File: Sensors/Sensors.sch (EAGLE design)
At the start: 32 parts, among them J2 JST_CONNECTOR, J6 JST_CONNECTOR, J7 JST_CONNECTOR, J8 JST_CONNECTOR, J9 JST_CONNECTOR

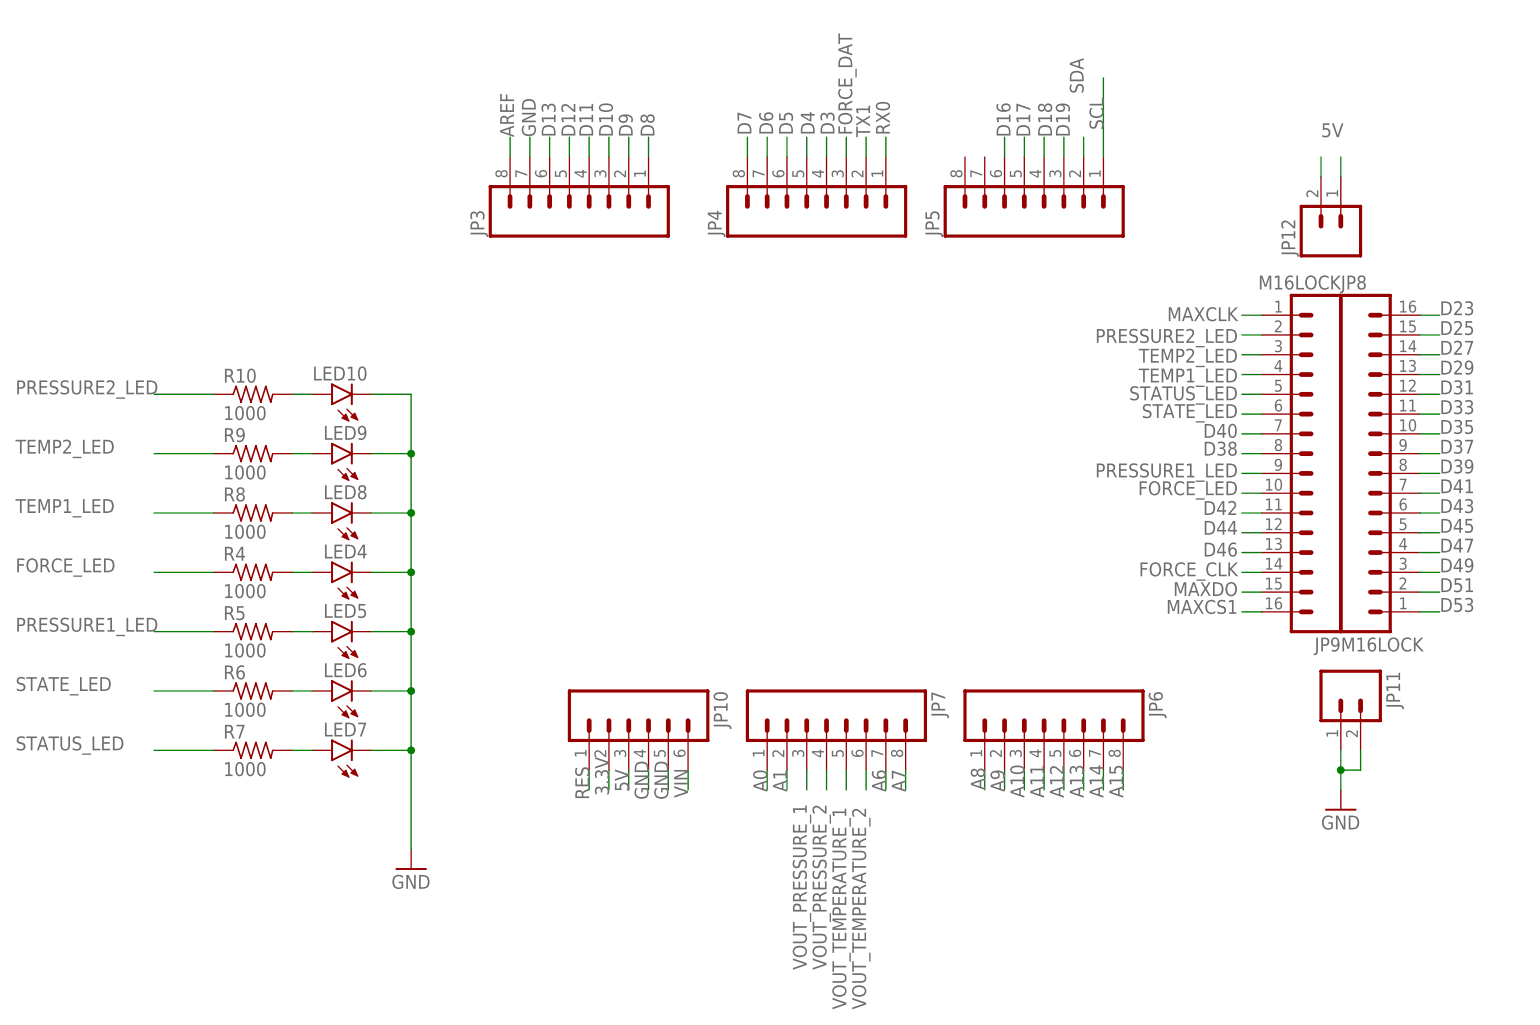
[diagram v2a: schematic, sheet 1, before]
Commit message: Finished routing, added accelerometer LED
UMN Logo is on wrong side, but such is life.
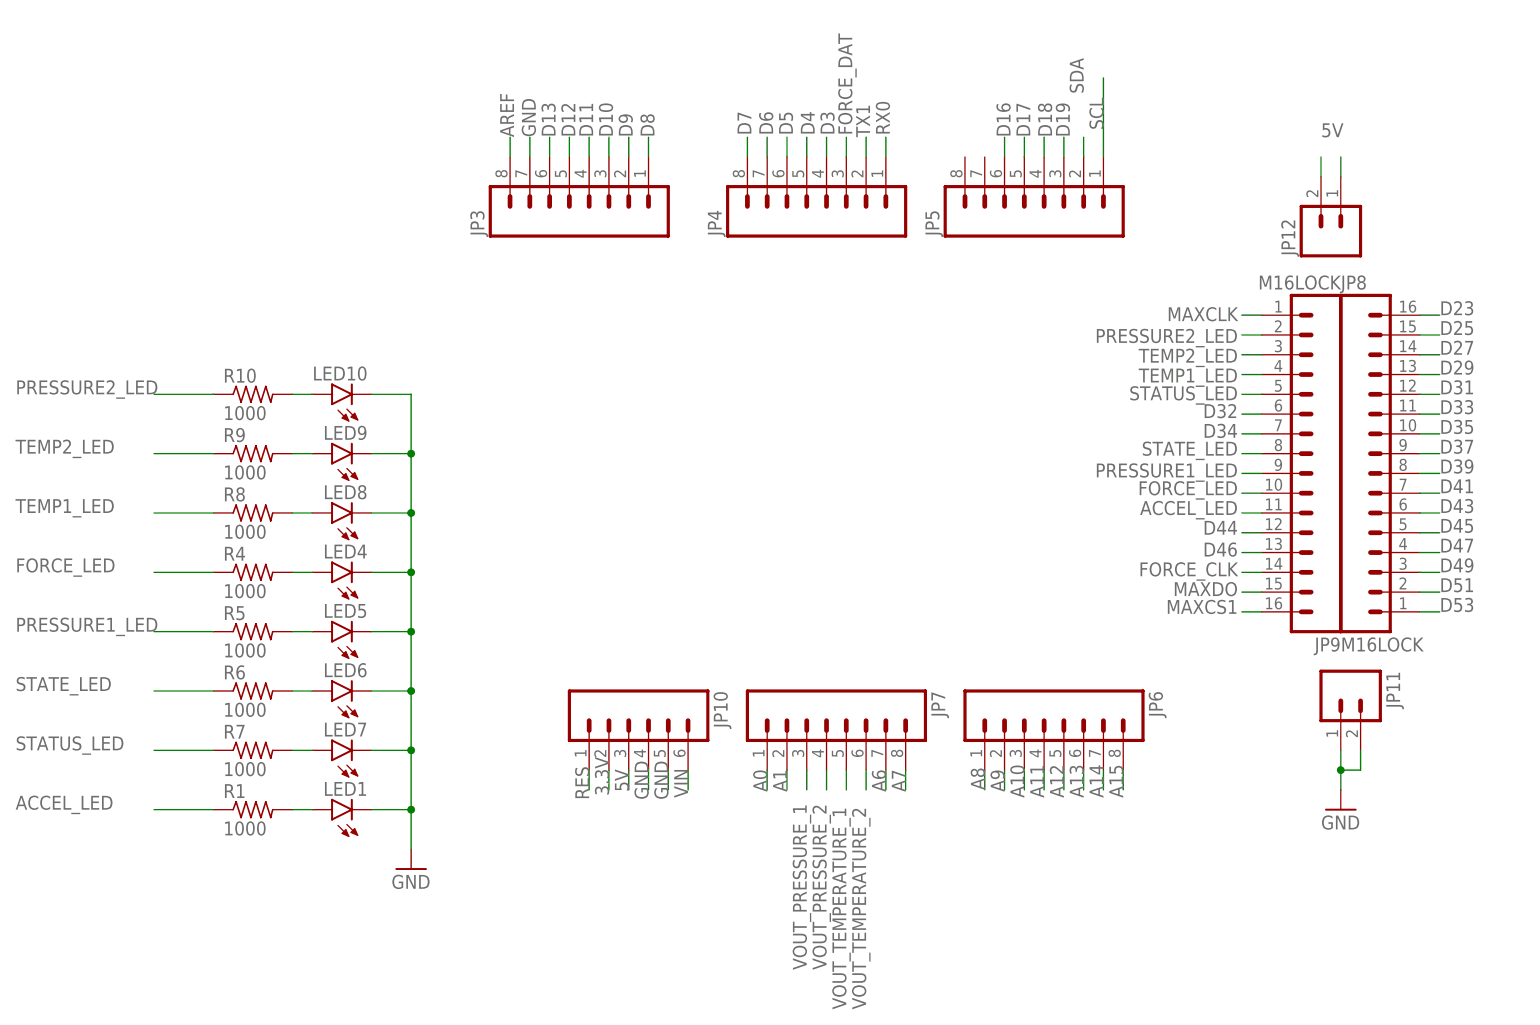
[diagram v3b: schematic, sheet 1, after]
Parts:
- added LED1: (no value), led:LED3MM
- added R1: 1000, rcl:R-US_0204/7
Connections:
- net D40 renamed D34
- removed net D38: JP9.8
- removed net D42: JP9.11
- new net ACCEL_LED: JP9.11, R1.1
- new net D32: JP9.6
- new net N$1: LED1.A, R1.2
- net GND: now also LED1.C
- net STATE_LED: now also JP9.8; no longer JP9.6

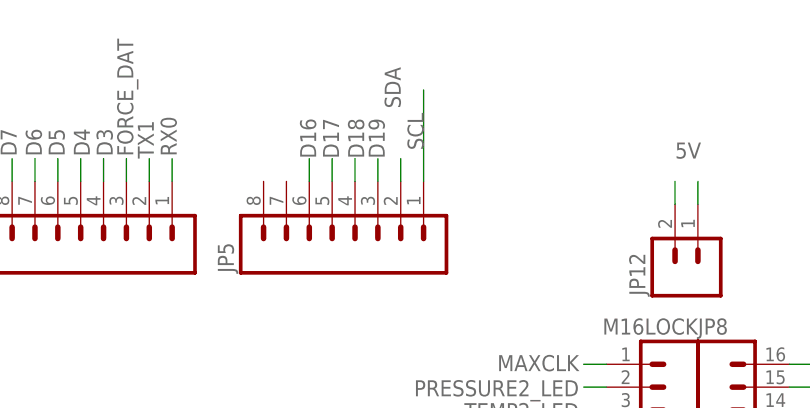
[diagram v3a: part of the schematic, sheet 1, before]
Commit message: Rearranged load cell seat, adressed errors
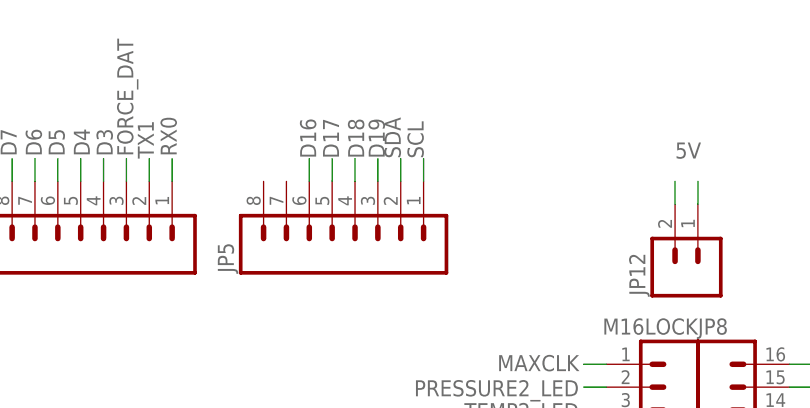
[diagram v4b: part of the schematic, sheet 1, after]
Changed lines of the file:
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@@
 <pinref part="JP5" gate="G$1" pin="2"/>
 <wire x1="144.78" y1="134.62" x2="144.78" y2="137.16" width="0.1524" layer="91"/>
-<label x="144.78" y="147.32" size="1.778" layer="95" rot="R90" align="bottom-right"/>
+<label x="144.78" y="137.16" size="1.778" layer="95" rot="R90"/>
 </segment>
 </net>
@@
 <segment>
 <pinref part="JP5" gate="G$1" pin="1"/>
-<wire x1="147.32" y1="134.62" x2="147.32" y2="144.78" width="0.1524" layer="91"/>
-<label x="147.32" y="142.24" size="1.778" layer="95" rot="R90" align="bottom-right"/>
+<wire x1="147.32" y1="134.62" x2="147.32" y2="137.16" width="0.1524" layer="91"/>
+<label x="147.32" y="137.16" size="1.778" layer="95" rot="R90"/>
 </segment>
 </net>

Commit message: Misc. minor tweaks to routing, layout and labels
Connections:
- net MAXCLK renamed D22
- net MAXCS1 renamed D52
- net MAXDO renamed D50
- net PRESSURE1_LED renamed PRESSURE_FUEL_LED
- net PRESSURE2_LED renamed PRESSURE_OX_LED
- net TEMP1_LED renamed TEMP_OUT_LED
- net TEMP2_LED renamed TEMP_IN_LED
- net VOUT_PRESSURE_1 renamed VOUT_PRESSURE_FUEL
- net VOUT_PRESSURE_2 renamed VOUT_PRESSURE_OX
- net VOUT_TEMPERATURE_1 renamed VOUT_TEMPERATURE_OUT
- net VOUT_TEMPERATURE_2 renamed VOUT_TEMPERATURE_IN
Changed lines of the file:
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@@
 <?xml version="1.0" encoding="utf-8"?>
 <!DOCTYPE eagle SYSTEM "eagle.dtd">
-<eagle version="9.5.1">
+<eagle version="9.4.0">
 <drawing>
 <settings>
@@
 </instance>
 <instance part="JP8" gate="G$1" x="177.8" y="96.52" smashed="yes">
-<attribute name="VALUE" x="177.8" y="71.12" size="1.778" layer="96"/>
+<attribute name="VALUE" x="180.34" y="71.12" size="1.778" layer="96"/>
 <attribute name="NAME" x="177.8" y="117.602" size="1.778" layer="95"/>
 </instance>
@@
 </segment>
 </net>
-<net name="VOUT_PRESSURE_1" class="0">
+<net name="VOUT_PRESSURE_FUEL" class="0">
 <segment>
 <wire x1="109.22" y1="53.34" x2="109.22" y2="55.88" width="0.1524" layer="91"/>
@@
 </segment>
 </net>
-<net name="VOUT_PRESSURE_2" class="0">
+<net name="VOUT_PRESSURE_OX" class="0">
 <segment>
 <wire x1="111.76" y1="53.34" x2="111.76" y2="55.88" width="0.1524" layer="91"/>
@@
 </segment>
 </net>
-<net name="VOUT_TEMPERATURE_1" class="0">
+<net name="VOUT_TEMPERATURE_OUT" class="0">
 <segment>
 <wire x1="114.3" y1="53.34" x2="114.3" y2="55.88" width="0.1524" layer="91"/>
@@
 </segment>
 </net>
-<net name="VOUT_TEMPERATURE_2" class="0">
+<net name="VOUT_TEMPERATURE_IN" class="0">
 <segment>
 <wire x1="116.84" y1="53.34" x2="116.84" y2="55.88" width="0.1524" layer="91"/>
@@
 </segment>
 </net>
-<net name="MAXCLK" class="0">
+<net name="D22" class="0">
 <segment>
 <wire x1="165.1" y1="114.3" x2="167.64" y2="114.3" width="0.1524" layer="91"/>
@@
 </segment>
 </net>
-<net name="MAXDO" class="0">
+<net name="D50" class="0">
 <segment>
 <wire x1="165.1" y1="78.74" x2="167.64" y2="78.74" width="0.1524" layer="91"/>
@@
 </segment>
 </net>
-<net name="MAXCS1" class="0">
+<net name="D52" class="0">
 <segment>
 <wire x1="165.1" y1="76.2" x2="167.64" y2="76.2" width="0.1524" layer="91"/>
@@
 </segment>
 </net>
-<net name="TEMP2_LED" class="0">
+<net name="TEMP_IN_LED" class="0">
 <segment>
 <pinref part="R9" gate="G$1" pin="1"/>
@@
 </segment>
 </net>
-<net name="PRESSURE1_LED" class="0">
+<net name="PRESSURE_FUEL_LED" class="0">
 <segment>
 <pinref part="R5" gate="G$1" pin="1"/>
@@
 </segment>
 </net>
-<net name="TEMP1_LED" class="0">
+<net name="TEMP_OUT_LED" class="0">
 <segment>
 <pinref part="R8" gate="G$1" pin="1"/>
@@
 </segment>
 </net>
-<net name="PRESSURE2_LED" class="0">
+<net name="PRESSURE_OX_LED" class="0">
 <segment>
 <pinref part="R10" gate="G$1" pin="1"/>
@@
 </segment>
 </net>
-<net name="VOUT_TEMPERATURE_1" class="0">
+<net name="VOUT_TEMPERATURE_OUT" class="0">
 <segment>
 <pinref part="J6" gate="G$1" pin="P2"/>
@@
 </segment>
 </net>
-<net name="VOUT_TEMPERATURE_2" class="0">
+<net name="VOUT_TEMPERATURE_IN" class="0">
 <segment>
 <pinref part="J7" gate="G$1" pin="P2"/>
@@
 </segment>
 </net>
-<net name="VOUT_PRESSURE_1" class="0">
+<net name="VOUT_PRESSURE_FUEL" class="0">
 <segment>
 <pinref part="J8" gate="G$1" pin="P2"/>
@@
 </segment>
 </net>
-<net name="VOUT_PRESSURE_2" class="0">
+<net name="VOUT_PRESSURE_OX" class="0">
 <segment>
 <pinref part="J9" gate="G$1" pin="P2"/>

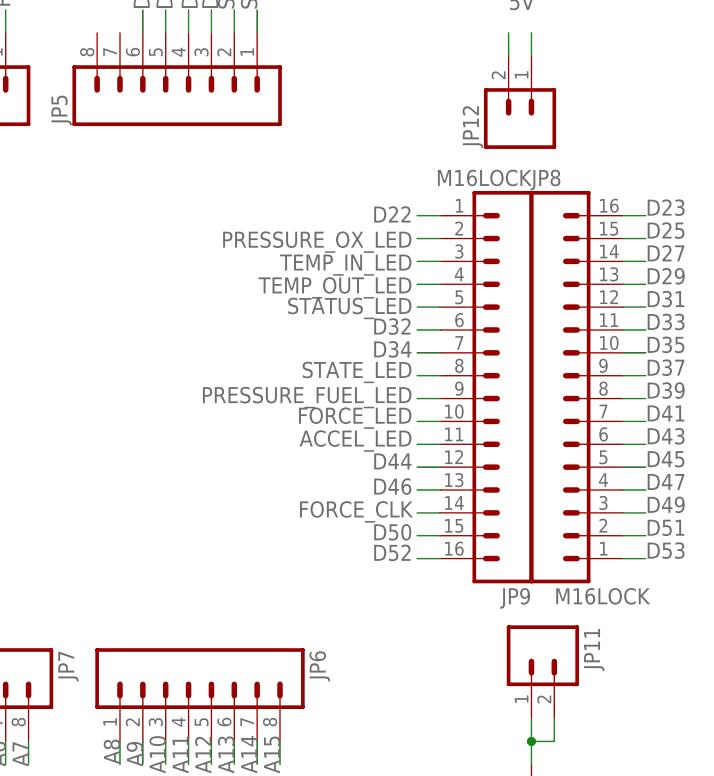
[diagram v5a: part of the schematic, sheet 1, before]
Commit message: Fix mistakes in sensors schematic
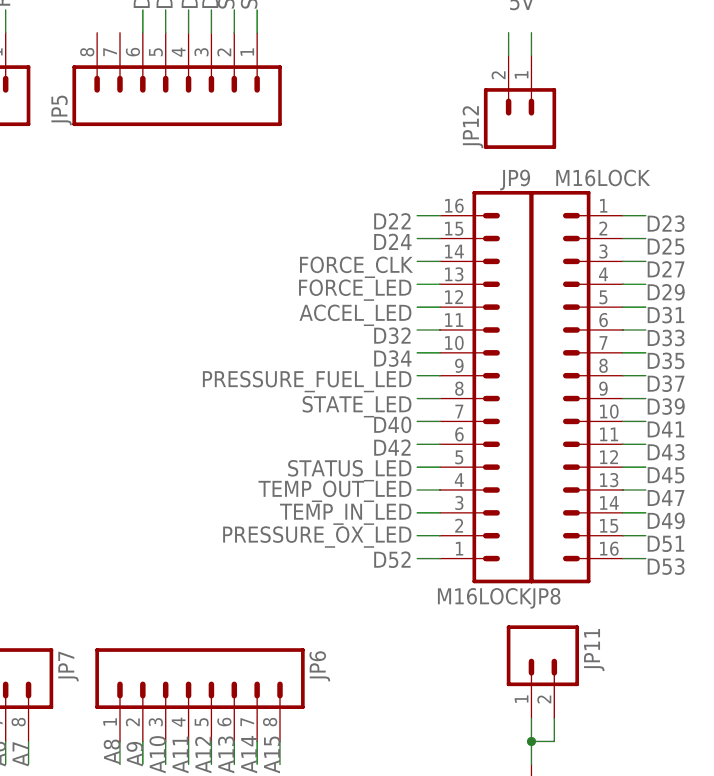
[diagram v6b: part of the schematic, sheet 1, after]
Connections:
- net D50 renamed D24
- removed net D44: JP9.12
- removed net D46: JP9.13
- new net D40: JP9.7
- new net D42: JP9.6
- net ACCEL_LED: now also JP9.12; no longer JP9.11
- net D22: now also JP9.16; no longer JP9.1
- net D23: now also JP8.1; no longer JP8.16
- net D25: now also JP8.2; no longer JP8.15
- net D27: now also JP8.3; no longer JP8.14
- net D29: now also JP8.4; no longer JP8.13
- net D31: now also JP8.5; no longer JP8.12
- net D32: now also JP9.11; no longer JP9.6
- net D33: now also JP8.6; no longer JP8.11
- net D34: now also JP9.10; no longer JP9.7
- net D35: now also JP8.7; no longer JP8.10
- net D37: now also JP8.8; no longer JP8.9
- net D39: now also JP8.9; no longer JP8.8
- net D41: now also JP8.10; no longer JP8.7
- net D43: now also JP8.11; no longer JP8.6
- net D45: now also JP8.12; no longer JP8.5
- net D47: now also JP8.13; no longer JP8.4
- net D49: now also JP8.14; no longer JP8.3
- net D51: now also JP8.15; no longer JP8.2
- net D52: now also JP9.1; no longer JP9.16
- net D53: now also JP8.16; no longer JP8.1
- net FORCE_LED: now also JP9.13; no longer JP9.10
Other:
- moved on the sheet: JP8, JP9

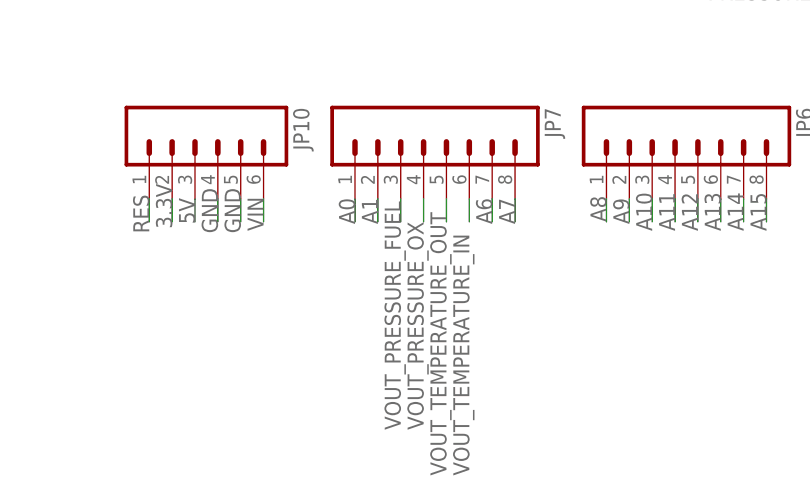
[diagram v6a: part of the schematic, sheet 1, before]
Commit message: Fix net naming error
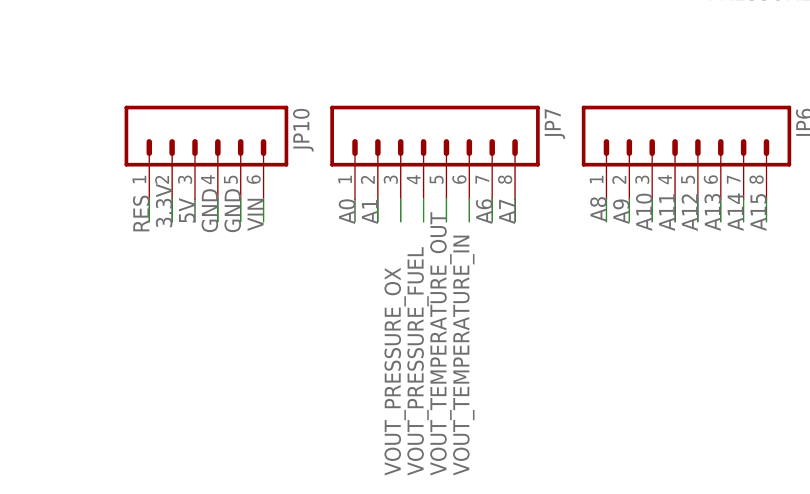
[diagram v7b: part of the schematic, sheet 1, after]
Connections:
- net VOUT_PRESSURE_FUEL: now also J9.P2, JP7.4; no longer J8.P2, JP7.3
- net VOUT_PRESSURE_OX: now also J8.P2, JP7.3; no longer J9.P2, JP7.4
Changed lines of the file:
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@@
+</segment>
+</net>
+<net name="VOUT_PRESSURE_OX" class="0">
+<segment>
+<wire x1="109.22" y1="53.34" x2="109.22" y2="55.88" width="0.1524" layer="91"/>
+<label x="109.22" y="25.146" size="1.778" layer="95" rot="R90"/>
+<pinref part="JP7" gate="G$1" pin="3"/>
 </segment>
 </net>
 <net name="VOUT_PRESSURE_FUEL" class="0">
 <segment>
-<wire x1="109.22" y1="53.34" x2="109.22" y2="55.88" width="0.1524" layer="91"/>
-<label x="109.22" y="30.226" size="1.778" layer="95" rot="R90"/>
-<pinref part="JP7" gate="G$1" pin="3"/>
-</segment>
-</net>
-<net name="VOUT_PRESSURE_OX" class="0">
-<segment>
 <wire x1="111.76" y1="53.34" x2="111.76" y2="55.88" width="0.1524" layer="91"/>
-<label x="111.76" y="30.226" size="1.778" layer="95" rot="R90"/>
+<label x="111.76" y="25.146" size="1.778" layer="95" rot="R90"/>
 <pinref part="JP7" gate="G$1" pin="4"/>
 </segment>
@@
 </segment>
 </net>
-<net name="VOUT_PRESSURE_FUEL" class="0">
+<net name="VOUT_PRESSURE_OX" class="0">
 <segment>
 <pinref part="J8" gate="G$1" pin="P2"/>
@@
 </segment>
 </net>
-<net name="VOUT_PRESSURE_OX" class="0">
+<net name="VOUT_PRESSURE_FUEL" class="0">
 <segment>
 <pinref part="J9" gate="G$1" pin="P2"/>

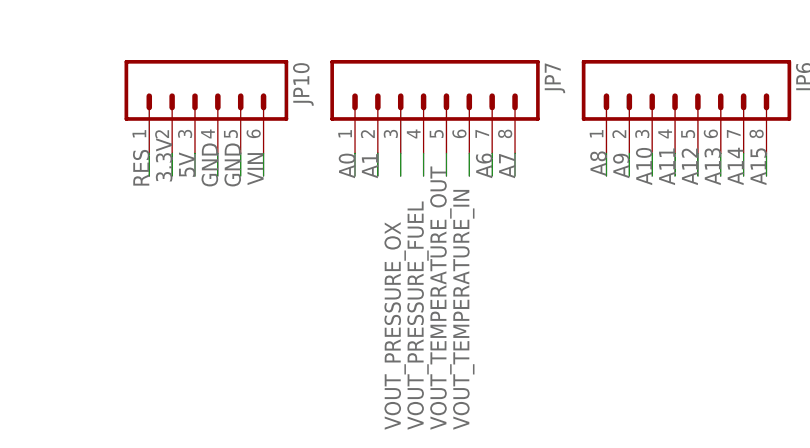
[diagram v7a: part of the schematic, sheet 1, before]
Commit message: Fix backwards pressure pin net names
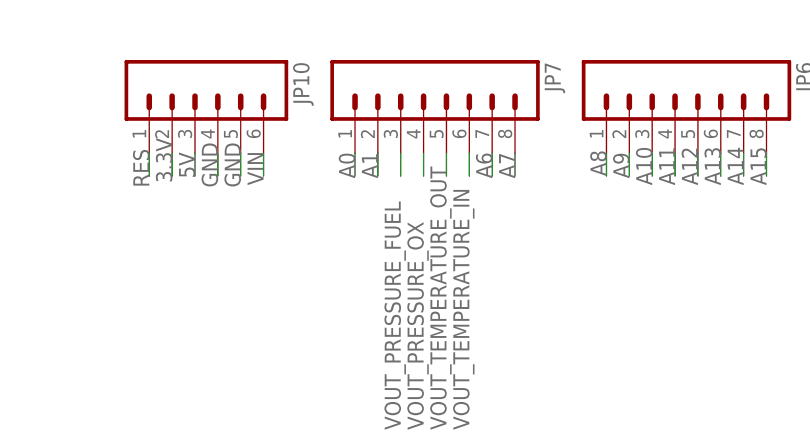
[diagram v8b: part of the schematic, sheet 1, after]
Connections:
- net VOUT_PRESSURE_FUEL: now also J8.P2, JP7.3; no longer J9.P2, JP7.4
- net VOUT_PRESSURE_OX: now also J9.P2, JP7.4; no longer J8.P2, JP7.3
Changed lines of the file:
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@@
 </segment>
 </net>
-<net name="VOUT_PRESSURE_OX" class="0">
+<net name="VOUT_PRESSURE_FUEL" class="0">
 <segment>
 <wire x1="109.22" y1="53.34" x2="109.22" y2="55.88" width="0.1524" layer="91"/>
@@
 </segment>
 </net>
-<net name="VOUT_PRESSURE_FUEL" class="0">
+<net name="VOUT_PRESSURE_OX" class="0">
 <segment>
 <wire x1="111.76" y1="53.34" x2="111.76" y2="55.88" width="0.1524" layer="91"/>
@@
 </segment>
 </net>
-<net name="VOUT_PRESSURE_OX" class="0">
+<net name="VOUT_PRESSURE_FUEL" class="0">
 <segment>
 <pinref part="J8" gate="G$1" pin="P2"/>
@@
 </segment>
 </net>
-<net name="VOUT_PRESSURE_FUEL" class="0">
+<net name="VOUT_PRESSURE_OX" class="0">
 <segment>
 <pinref part="J9" gate="G$1" pin="P2"/>
